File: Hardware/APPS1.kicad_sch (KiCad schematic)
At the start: 15 parts, among them U8 MCP6N11-001E/SN

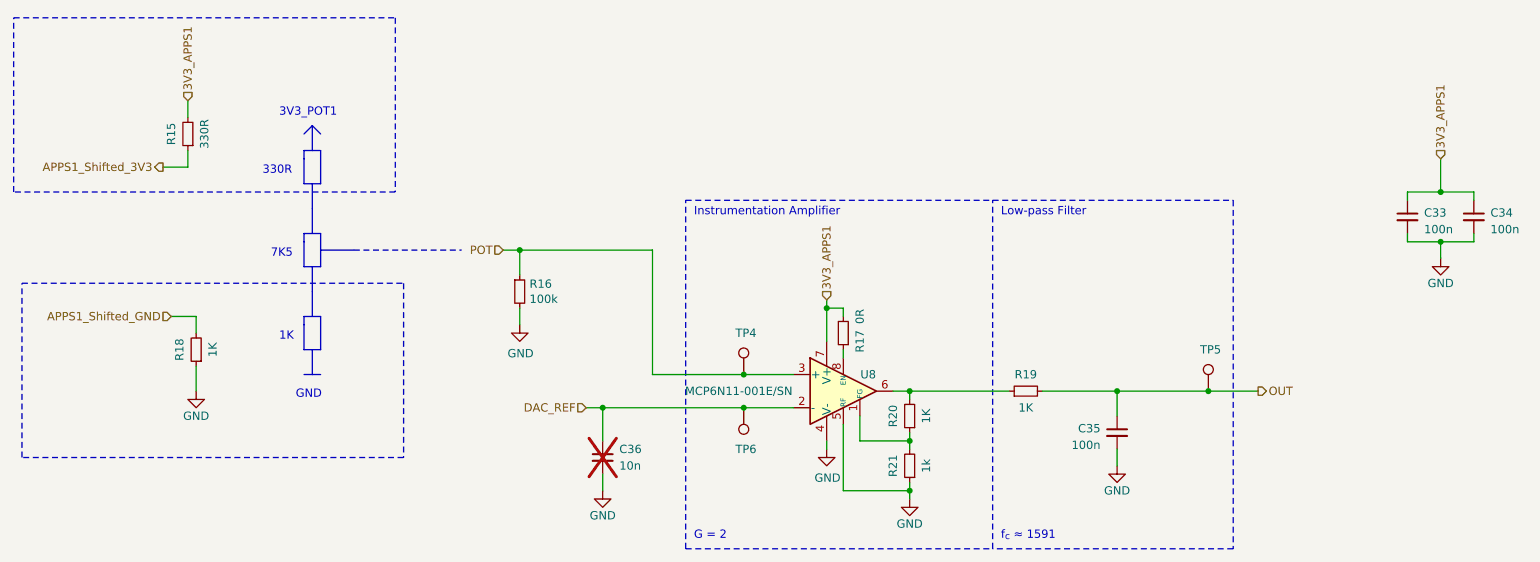
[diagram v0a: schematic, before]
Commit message: Changes in schematic, separated CAN buses, added XIAO Sense S3 DevBoard
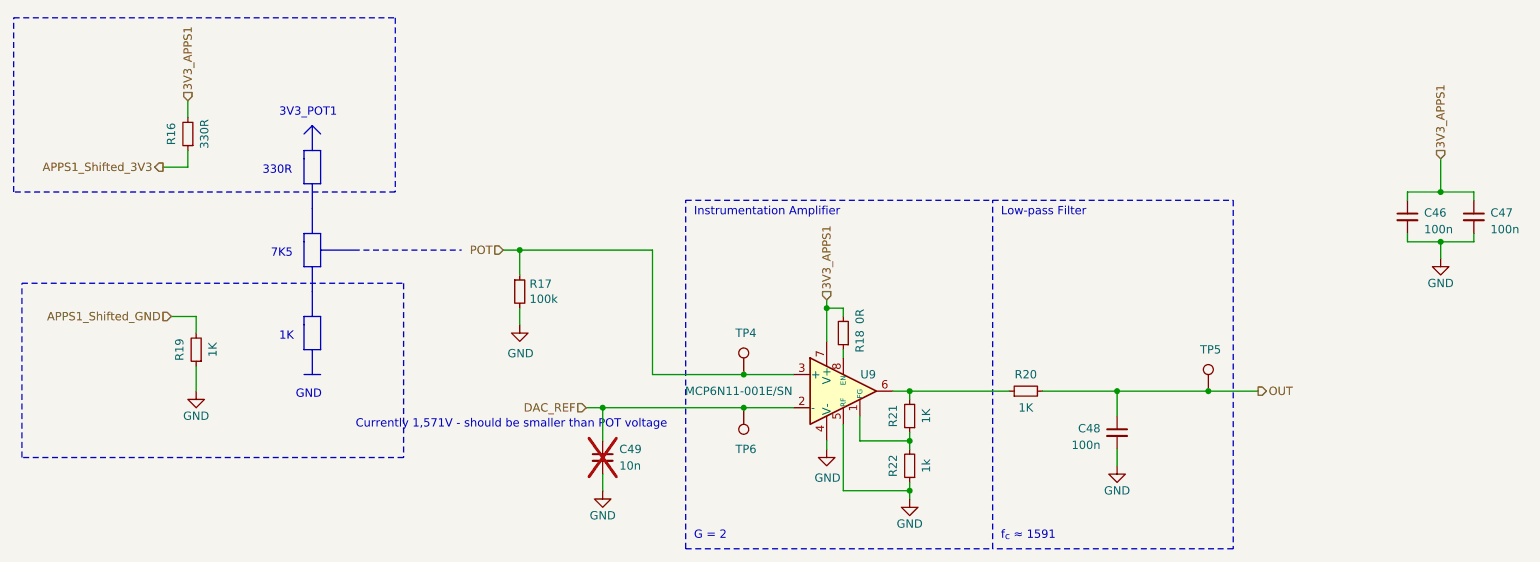
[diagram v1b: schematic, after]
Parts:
- renumbered C33 to C46, C34 to C47, C35 to C48, C36 to C49, R15 to R16, R16 to R17, R17 to R18, R18 to R19, R19 to R20, R20 to R21, R21 to R22, U8 to U9
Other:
- note added: "Currently 1,571V - should be smaller than POT voltage"

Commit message: Changes in CAN section
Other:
- title: (none) -> FrontBox
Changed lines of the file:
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@@
 	(generator_version "9.0")
 	(paper "A4")
+	(title_block
+		(title "FrontBox")
+	)
 	(rectangle
 		(start 29.21 38.1)

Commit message: BOM update
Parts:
- C46, C47, C48, C49, R16, R17, R18, R19, R20, R21, R22: Mouser Part Number (none) -> .
- U9: Mouser Part Number (none) -> 579-MCP6N11-001E/SN
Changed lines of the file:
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@@
+			)
+		)
+		(property "Mouser Part Number" "."
+			(at 55.88 55.88 0)
+			(effects
+				(font
+					(size 1.27 1.27)
+				)
 			)
 		)
@@
 		)
 		(property "Description" ""
+			(at 156.21 95.25 0)
+			(effects
+				(font
+					(size 1.27 1.27)
+				)
+				(hide yes)
+			)
+		)
+		(property "Mouser Part Number" "579-MCP6N11-001E/SN"
 			(at 156.21 95.25 0)
 			(effects
@@
 			)
 		)
+		(property "Mouser Part Number" "."
+			(at 198.12 101.6 0)
+			(effects
+				(font
+					(size 1.27 1.27)
+				)
+			)
+		)
 		(pin "1"
 		)
@@
 			)
 		)
+		(property "Mouser Part Number" "."
+			(at 57.15 88.9 0)
+			(effects
+				(font
+					(size 1.27 1.27)
+				)
+			)
+		)
 		(pin "1"
 		)
@@
 				)
 				(hide yes)
+			)
+		)
+		(property "Mouser Part Number" "."
+			(at 166.37 99.06 0)
+			(effects
+				(font
+					(size 1.27 1.27)
+				)
 			)
 		)
@@
 			)
 		)
+		(property "Mouser Part Number" "."
+			(at 119.38 105.41 0)
+			(effects
+				(font
+					(size 1.27 1.27)
+				)
+			)
+		)
 		(pin "1"
 		)
@@
 			)
 		)
+		(property "Mouser Part Number" "."
+			(at 106.68 80.01 0)
+			(effects
+				(font
+					(size 1.27 1.27)
+				)
+			)
+		)
 		(pin "1"
 		)
@@
 			)
 		)
+		(property "Mouser Part Number" "."
+			(at 184.15 95.25 0)
+			(effects
+				(font
+					(size 1.27 1.27)
+				)
+			)
+		)
 		(pin "1"
 		)
@@
 			)
 		)
+		(property "Mouser Part Number" "."
+			(at 242.57 68.58 0)
+			(effects
+				(font
+					(size 1.27 1.27)
+				)
+			)
+		)
 		(pin "1"
 		)
@@
 			)
 		)
+		(property "Mouser Part Number" "."
+			(at 156.21 86.36 0)
+			(effects
+				(font
+					(size 1.27 1.27)
+				)
+			)
+		)
 		(pin "1"
 		)
@@
 			)
 		)
+		(property "Mouser Part Number" "."
+			(at 166.37 106.68 0)
+			(effects
+				(font
+					(size 1.27 1.27)
+				)
+			)
+		)
 		(pin "1"
 		)
@@
 			)
 		)
+		(property "Mouser Part Number" "."
+			(at 252.73 68.58 0)
+			(effects
+				(font
+					(size 1.27 1.27)
+				)
+			)
+		)

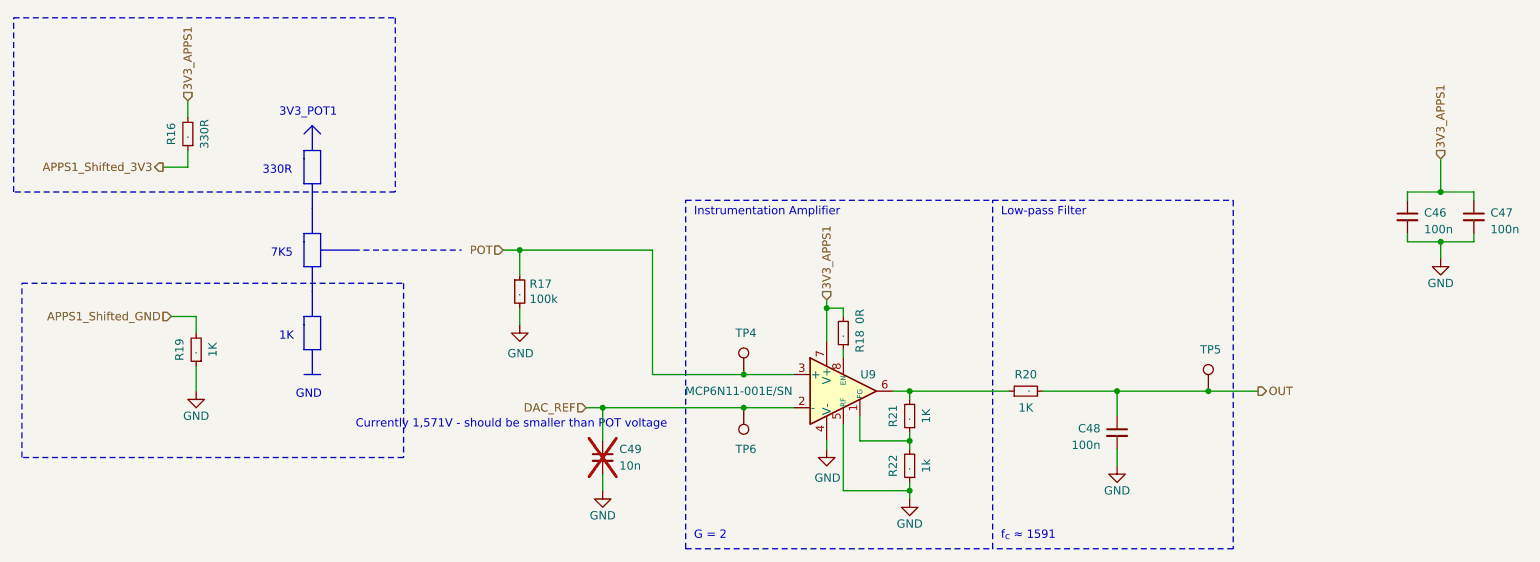
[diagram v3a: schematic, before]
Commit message: Added tensionmeter section, updated APPS resistors for transfer function
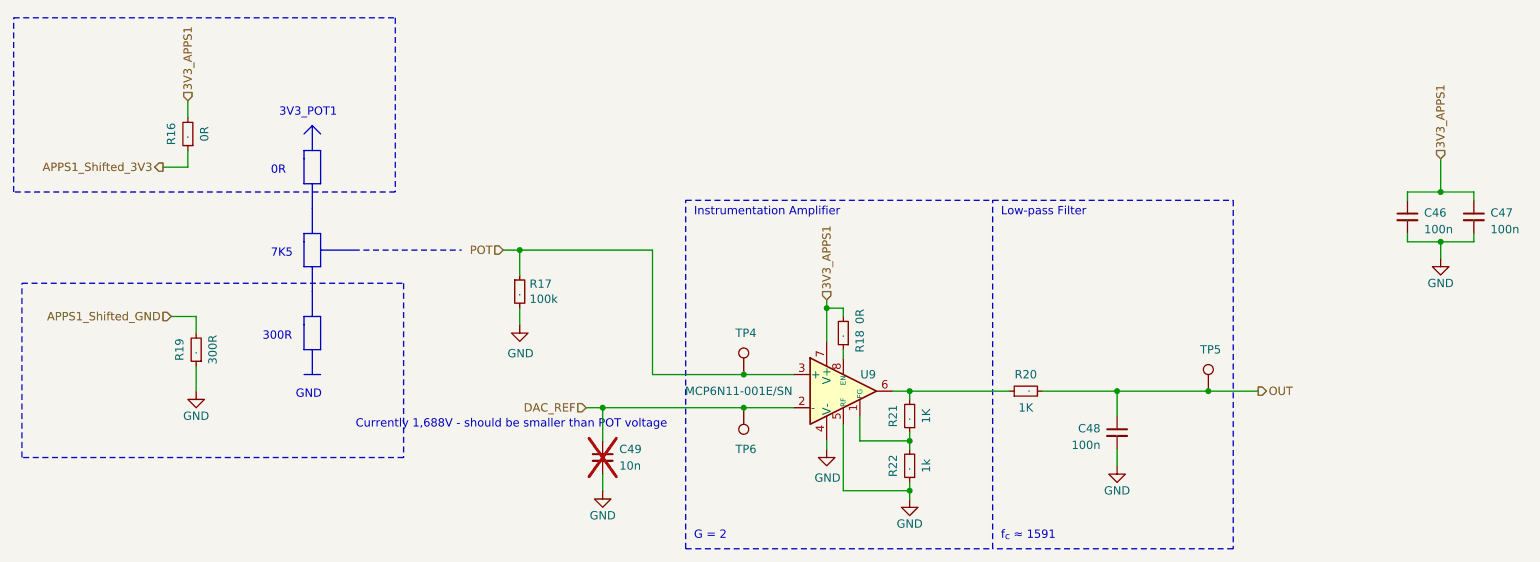
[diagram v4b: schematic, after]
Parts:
- R16: value 330R -> 0R
- R19: value 1K -> 300R
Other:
- note added: "0R"
- note added: "300R"
- note added: "Currently 1,688V - should be smaller than POT voltage"
- note removed: "1K"
- note removed: "330R"
- note removed: "Currently 1,571V - should be smaller than POT voltage"
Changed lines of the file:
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@@
 		)
 	)
-	(text "Currently 1,571V - should be smaller than POT voltage\n"
+	(text "Currently 1,688V - should be smaller than POT voltage\n"
 		(exclude_from_sim no)
 		(at 105.41 100.33 0)
@@
 		)
 	)
-	(text "1K"
-		(exclude_from_sim no)
-		(at 69.85 87.63 0)
+	(text "300R\n"
+		(exclude_from_sim no)
+		(at 67.31 87.63 0)
 		(effects
 			(font
@@
 		)
 	)
-	(text "330R"
-		(exclude_from_sim no)
-		(at 67.31 62.23 0)
+	(text "0R"
+		(exclude_from_sim no)
+		(at 68.58 62.23 0)
 		(effects
 			(font
@@
 			)
 		)
-		(property "Value" "330R"
+		(property "Value" "0R"
 			(at 58.42 55.88 90)
 			(effects
@@
 			)
 		)
-		(property "Value" "1K"
+		(property "Value" "300R"
 			(at 59.69 88.9 90)
 			(effects
